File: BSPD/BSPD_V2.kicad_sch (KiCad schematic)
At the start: 36 parts, among them J1 Conn_01x02_Socket, J2 Conn_01x02_Socket, J3 Conn_01x02_Socket, J4 Conn_01x02_Socket, K1 Fujitsu_FTR-LYCA005x, Q2 NPN, Q3 IRF540N, Q4 NPN, U1 74LS02, U2 74LS08, U3 LM393, U5 LM393

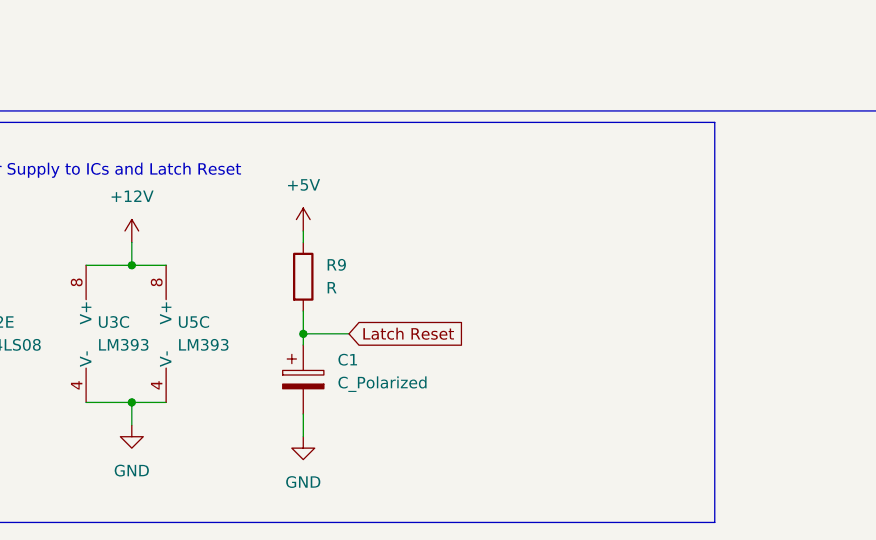
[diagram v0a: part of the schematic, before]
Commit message: Added a bypass capacitor to the supply of the comparators as stated by the Datasheet.
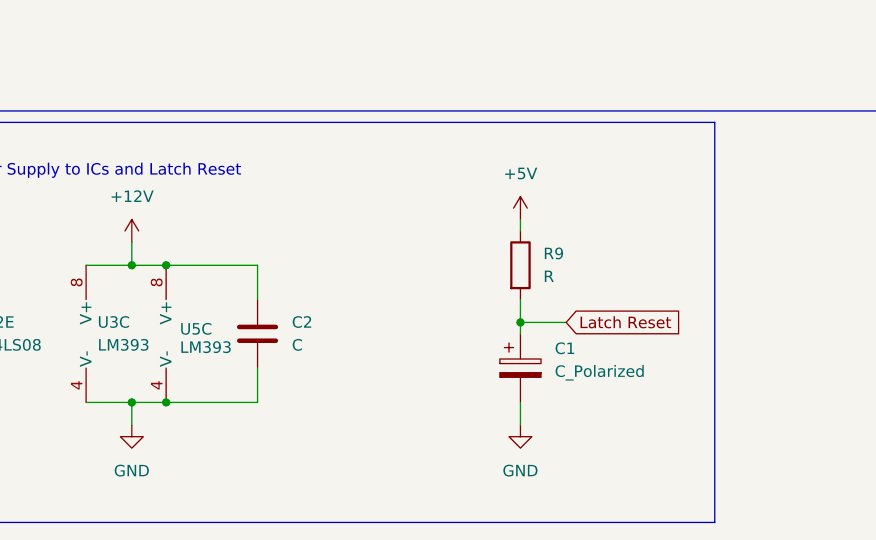
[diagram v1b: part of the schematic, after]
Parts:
- added C2: C, symbol Device:C
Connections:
- net +12V: now also C2.1
- net GND: now also C2.2
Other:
- moved on the sheet: C1, R9
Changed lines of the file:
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@@
 	)
 	(junction
+		(at 69.85 182.88)
+		(diameter 0)
+		(color 0 0 0 0)
+	)
+	(junction
 		(at 200.66 46.99)
 		(diameter 0)
@@
 	)
 	(junction
-		(at 85.09 175.26)
+		(at 69.85 167.64)
+		(diameter 0)
+		(color 0 0 0 0)
+	)
+	(junction
+		(at 109.22 173.99)
 		(diameter 0)
 		(color 0 0 0 0)
@@
 	(wire
 		(pts
-			(xy 85.09 175.26) (xy 85.09 176.53)
+			(xy 109.22 173.99) (xy 109.22 175.26)
 		)
 		(stroke
@@
 	(wire
 		(pts
+			(xy 69.85 167.64) (xy 80.01 167.64)
+		)
+		(stroke
+			(width 0)
+			(type default)
+		)
+	)
+	(wire
+		(pts
 			(xy 34.29 187.96) (xy 43.18 187.96)
 		)
@@
 	(wire
 		(pts
-			(xy 85.09 184.15) (xy 85.09 186.69)
+			(xy 109.22 182.88) (xy 109.22 185.42)
 		)
 		(stroke
@@
 	(wire
 		(pts
-			(xy 85.09 175.26) (xy 90.17 175.26)
+			(xy 109.22 173.99) (xy 114.3 173.99)
 		)
 		(stroke
@@
 	(wire
 		(pts
-			(xy 85.09 163.83) (xy 85.09 165.1)
+			(xy 109.22 162.56) (xy 109.22 163.83)
 		)
 		(stroke
@@
 	(wire
 		(pts
-			(xy 85.09 172.72) (xy 85.09 175.26)
+			(xy 109.22 171.45) (xy 109.22 173.99)
 		)
 		(stroke
@@
 	(wire
 		(pts
+			(xy 69.85 182.88) (xy 80.01 182.88)
+		)
+		(stroke
+			(width 0)
+			(type default)
+		)
+	)
+	(wire
+		(pts
 			(xy 191.77 154.94) (xy 194.31 154.94)
 		)
@@
 	(wire
 		(pts
+			(xy 80.01 167.64) (xy 80.01 171.45)
+		)
+		(stroke
+			(width 0)
+			(type default)
+		)
+	)
+	(wire
+		(pts
 			(xy 30.48 107.95) (xy 40.64 107.95)
 		)
@@
 	(wire
 		(pts
+			(xy 80.01 179.07) (xy 80.01 182.88)
+		)
+		(stroke
+			(width 0)
+			(type default)
+		)
+	)
+	(wire
+		(pts
 			(xy 116.84 104.14) (xy 116.84 106.68)
 		)
@@
 	(global_label "Latch Reset"
 		(shape input)
-		(at 90.17 175.26 0)
+		(at 114.3 173.99 0)
 		(fields_autoplaced yes)
 		(effects
@@
 		)
 		(property "Intersheetrefs" "${INTERSHEET_REFS}"
-			(at 104.4642 175.26 0)
+			(at 128.5942 173.99 0)
 			(effects
 				(font
@@
 	)
 	(symbol
+		(lib_id "Device:C")
+		(at 80.01 175.26 0)
+		(unit 1)
+		(exclude_from_sim no)
+		(in_bom yes)
+		(on_board yes)
+		(dnp no)
+		(fields_autoplaced yes)
+		(property "Reference" "C2"
+			(at 83.82 173.9899 0)
+			(effects
+				(font
+					(size 1.27 1.27)
+				)
+				(justify left)
+			)
+		)
+		(property "Value" "C"
+			(at 83.82 176.5299 0)
+			(effects
+				(font
+					(size 1.27 1.27)
+				)
+				(justify left)
+			)
+		)
+		(property "Footprint" ""
+			(at 80.9752 179.07 0)
+			(effects
+				(font
+					(size 1.27 1.27)
+				)
+				(hide yes)
+			)
+		)
+		(property "Datasheet" "~"
+			(at 80.01 175.26 0)
+			(effects
+				(font
+					(size 1.27 1.27)
+				)
+				(hide yes)
+			)
+		)
+		(property "Description" "Unpolarized capacitor"
+			(at 80.01 175.26 0)
+			(effects
+				(font
+					(size 1.27 1.27)
+				)
+				(hide yes)
+			)
+		)
+		(pin "1"
+		)
+		(pin "2"
+		)
+		(instances
+			(project ""
+				(path "/d92b65b7-5ac6-4942-9c7f-8311f0326af7"
+					(reference "C2")
+					(unit 1)
+				)
+			)
+		)
+	)
+	(symbol
 		(lib_id "power:+12V")
 		(at 232.41 22.86 0)
@@
 	(symbol
 		(lib_id "power:GND")
-		(at 85.09 186.69 0)
+		(at 109.22 185.42 0)
 		(unit 1)
 		(exclude_from_sim no)
@@
 		(fields_autoplaced yes)
 		(property "Reference" "#PWR010"
-			(at 85.09 193.04 0)
+			(at 109.22 191.77 0)
 			(effects
 				(font
@@
 		)
 		(property "Value" "GND"
-			(at 85.09 191.77 0)
+			(at 109.22 190.5 0)
 			(effects
 				(font
@@
 		)
 		(property "Footprint" ""
-			(at 85.09 186.69 0)
+			(at 109.22 185.42 0)
 			(effects
 				(font
@@
 		)
 		(property "Datasheet" ""
-			(at 85.09 186.69 0)
+			(at 109.22 185.42 0)
 			(effects
 				(font
@@
 		)
 		(property "Description" "Power symbol creates a global label with name \"GND\" , ground"
-			(at 85.09 186.69 0)
+			(at 109.22 185.42 0)
 			(effects
 				(font
@@
 	(symbol
 		(lib_id "power:+5V")
-		(at 85.09 163.83 0)
+		(at 109.22 162.56 0)
 		(unit 1)
 		(exclude_from_sim no)
@@
 		(fields_autoplaced yes)
 		(property "Reference" "#PWR09"
-			(at 85.09 167.64 0)
+			(at 109.22 166.37 0)
 			(effects
 				(font
@@
 		)
 		(property "Value" "+5V"
-			(at 85.09 158.75 0)
+			(at 109.22 157.48 0)
 			(effects
 				(font
@@
 		)
 		(property "Footprint" ""
-			(at 85.09 163.83 0)
+			(at 109.22 162.56 0)
 			(effects
 				(font
@@
 		)
 		(property "Datasheet" ""
-			(at 85.09 163.83 0)
+			(at 109.22 162.56 0)
 			(effects
 				(font
@@
 		)
 		(property "Description" "Power symbol creates a global label with name \"+5V\""
-			(at 85.09 163.83 0)
+			(at 109.22 162.56 0)
 			(effects
 				(font
@@
 	(symbol
 		(lib_id "Device:R")
-		(at 85.09 168.91 0)
+		(at 109.22 167.64 0)
 		(unit 1)
 		(exclude_from_sim no)
@@
 		(fields_autoplaced yes)
 		(property "Reference" "R9"
-			(at 87.63 167.6399 0)
+			(at 111.76 166.3699 0)
 			(effects
 				(font
@@
 		)
 		(property "Value" "R"
-			(at 87.63 170.1799 0)
+			(at 111.76 168.9099 0)
 			(effects
 				(font
@@
 		)
 		(property "Footprint" ""
-			(at 83.312 168.91 90)
+			(at 107.442 167.64 90)
 			(effects
 				(font
@@
 		)
 		(property "Datasheet" "~"
-			(at 85.09 168.91 0)
+			(at 109.22 167.64 0)
 			(effects
 				(font
@@
 		)
 		(property "Description" "Resistor"
-			(at 85.09 168.91 0)
+			(at 109.22 167.64 0)
 			(effects
 				(font
@@
 	(symbol
 		(lib_id "Device:C_Polarized")
-		(at 85.09 180.34 0)
+		(at 109.22 179.07 0)
 		(unit 1)
 		(exclude_from_sim no)
@@
 		(fields_autoplaced yes)
 		(property "Reference" "C1"
-			(at 88.9 178.1809 0)
+			(at 113.03 176.9109 0)
 			(effects
 				(font
@@
 		)
 		(property "Value" "C_Polarized"
-			(at 88.9 180.7209 0)
+			(at 113.03 179.4509 0)
 			(effects
 				(font
@@
 		)
 		(property "Footprint" ""
-			(at 86.0552 184.15 0)
+			(at 110.1852 182.88 0)
 			(effects
 				(font
@@
 		)
 		(property "Datasheet" "~"
-			(at 85.09 180.34 0)
+			(at 109.22 179.07 0)
 			(effects
 				(font
@@
 		)
 		(property "Description" "Polarized capacitor"
-			(at 85.09 180.34 0)
+			(at 109.22 179.07 0)
 			(effects
 				(font
@@
 		(on_board yes)
 		(dnp no)
-		(fields_autoplaced yes)
 		(property "Reference" "U5"
-			(at 71.12 173.9899 0)
+			(at 71.374 174.752 0)
 			(effects
 				(font
@@
 		)
 		(property "Value" "LM393"
-			(at 71.12 176.5299 0)
+			(at 71.374 176.784 0)
 			(effects
 				(font

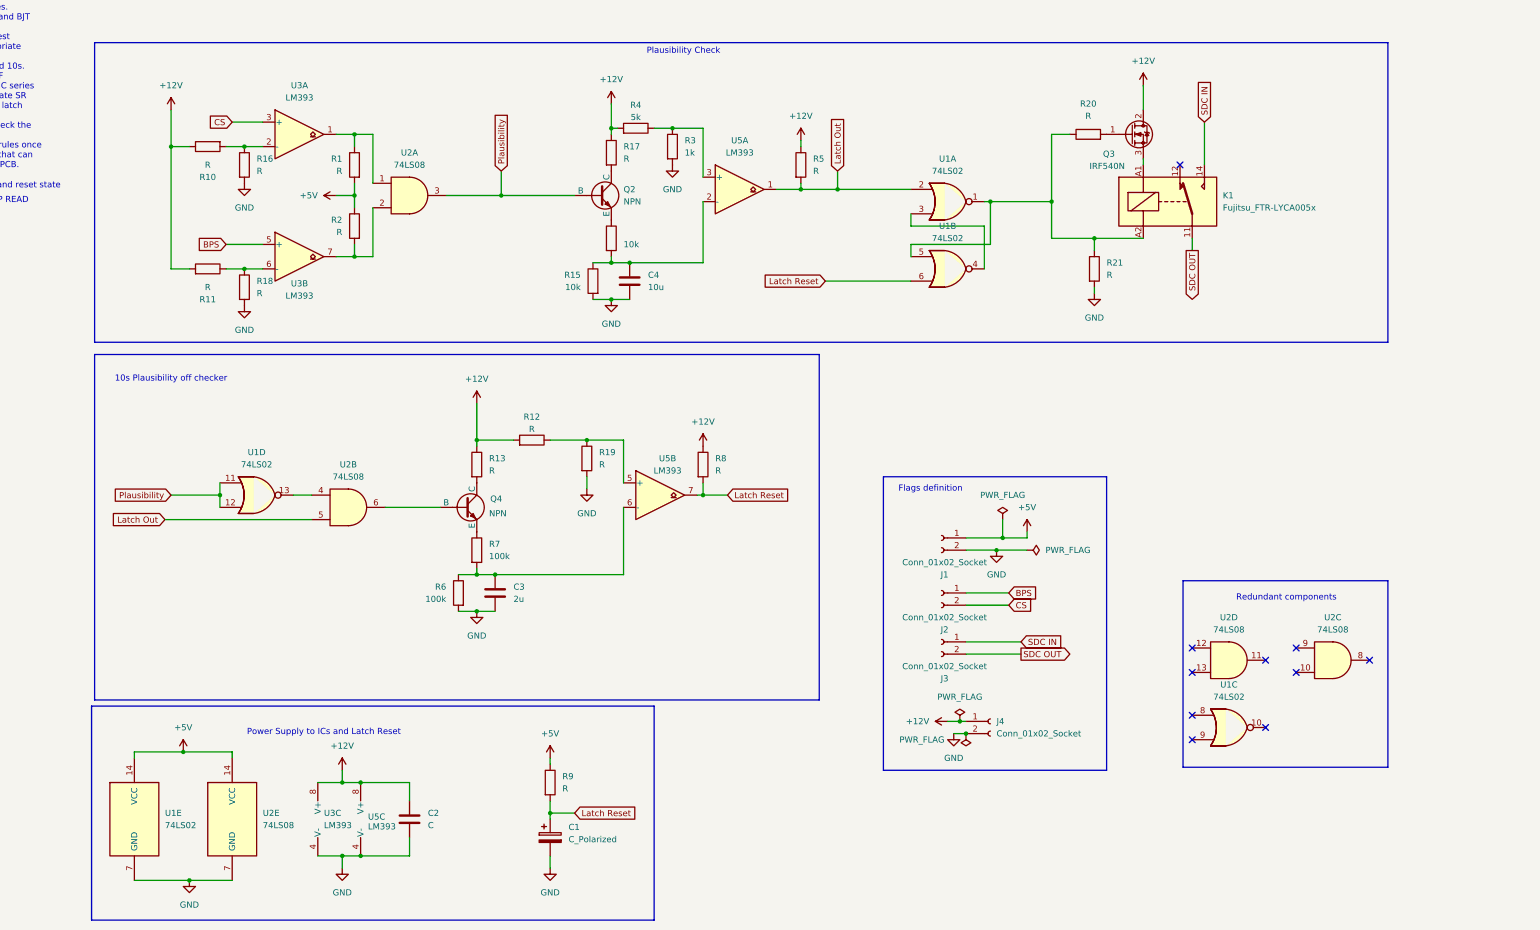
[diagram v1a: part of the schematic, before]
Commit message: Added a CD4081BM in place of regular LS AND gates, reason being better Voltage Supply range(3V-18V) which allows it to use the GLV power supply directly. Also, lower Tp. Had to add some flags as the symbol didn't break up into individual gates.
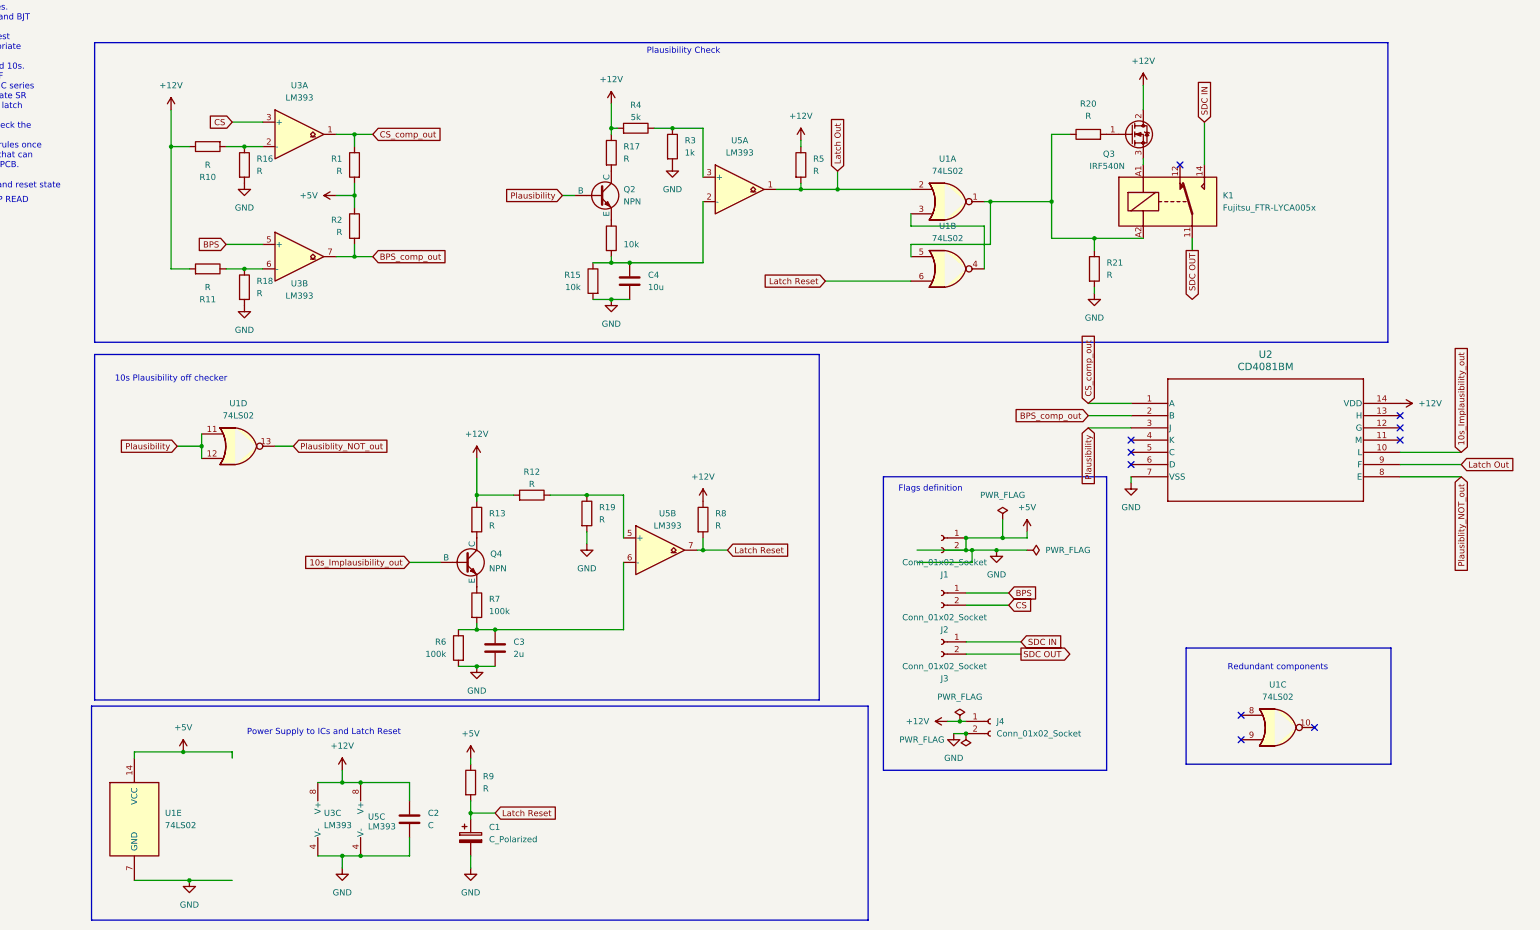
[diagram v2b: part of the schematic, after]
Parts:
- removed U2: 74LS08, symbol 74xx:74LS08
- added U2: CD4081BM, D14, symbol CD4081B:CD4081BM
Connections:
- net GND is gone; now on net +5V: C1.2, C2.2, C3.2, C4.2, J1.2 (Pin_2), J4.2 (Pin_2), R15.2, R16.2, R18.2, R19.2, R21.2, R3.2, R6.2, U1.7 (GND), U3.4 (V-), U5.4 (V-)
- net +12V: now also U2.14 (VDD)
- net +5V: now also U2.7 (VSS)
- net Latch Out: now also U2.9 (F)
- net Plausibility: now also U2.3 (J)
- net CS_comp_out: now reaches R1.1, U3.1
- net CS_comp_out: now also U2.1 (A)
- net 10s_Implausibility_out: now reaches Q4.2 (B)
- net 10s_Implausibility_out: now also U2.10 (L)
- net Plausiblity_NOT_out: now reaches U1.13
- net Plausiblity_NOT_out: now also U2.8 (E)
- net BPS_comp_out: now reaches R2.2, U3.7
- net BPS_comp_out: now also U2.2 (B)
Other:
- moved on the sheet: C1, C3, Q4, R12, R13, R19, R6, R7, R8, R9, U1C, U1D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

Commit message: Added the higher voltage NOR gate CD4001B IC, cleaned the schematic, and also added the inputs/ouputs to the symbols of the imported ics (CD4001B and CD40081B). Removed all +5V pins from the schematic.
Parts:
- removed J1: Conn_01x02_Socket, symbol Connector:Conn_01x02_Socket
- removed U1: 74LS02, symbol 74xx:74LS02
- removed U2: CD4081BM, D14, symbol CD4081B:CD4081BM
- added U1, U2: CD4001BM, D14, symbol CD4001B:CD4001BM
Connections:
- net +12V: now also R1.2, R2.1, R9.1, U1.14 (VDD), U2.14 (VDD)
- net 10s_Implausibility_out: now also U2.10 (L)
- net BPS_comp_out: now also U2.2 (B)
- net CS_comp_out: now also U2.1 (A)
- net Latch Out: now also U1.1 (A), U2.9 (F)
- net Latch Reset: now also U1.6 (D)
- net Plausibility: now also U1.8 (E), U1.9 (F), U2.3 (J)
- net Plausiblity_NOT_out: now also U1.10 (L), U2.8 (E)
- net Q_ouput: now reaches K1.A2, R20.1, R21.1
- net Q_ouput: now also U1.3 (J), U1.5 (C)
- net +5V renamed GND
- net GND: now also U1.7 (VSS), U2.7 (VSS); no longer R1.2, R2.1, R9.1
- new net: U1.2 (B), U1.4 (K)
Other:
- note added: "1)Check the voltage divider values for 2.2V to 10.5V from CS. 2)Get the pullup resistor values. 3)Compare between MOSFET and BJT as switch. 4)Check for whatever is the best and for that place the appropriate resistors to bias them. 5)Verify the time of 500ms and 10s. Keep capacitor value of 0.1uF 7)Look into reset for the nor gate SR Latch. 8)After finishing the above, check the logic once again.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"
- note added: "AND GATE"
- note added: "NOR GATE"
- note removed: "1)Check the voltage divider values for 2.2V to 10.5V from CS. 2)Get the pullup resistor values. 3)Compare between MOSFET and BJT as switch. 4)Check for whatever is the best and for that place the appropriate resistors to bias them. 5)Verify the time of 500ms and 10s. Keep capacitor value of 0.1uF 6)Replace the LS series with HC series 7)Look into reset for the nor gate SR Latch. If possible, repl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"
- note removed: "Redundant components"
- note removed: "Relay and reset state"
- note removed: "SCS IMP READ"
- moved on the sheet: C1, C2, C3, C4, J2, J3, J4, K1, Q2, Q3, Q4, R1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

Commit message: Changed the PS capcitor value to 1uF, it should be enough for removing inconsistencies in the GLV supply. Also set the pulldown resistor value to 1 ohm, it needs to be as small as possible to keep the SR state zero as fast as possible, this may need to be revised depending on the review
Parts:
- removed Q2: NPN, symbol Simulation_SPICE:NPN
- added Q1: NPN, symbol Simulation_SPICE:NPN
- C2: value C -> 1uF
- R21: value R -> 1
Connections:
- net Plausibility: now also Q1.2 (B)
- net at R17.2: now also Q1.1 (C)
- net at R14.1: now also Q1.3 (E)
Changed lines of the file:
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@@
 	(wire
 		(pts
-			(xy 137.16 69.85) (xy 139.7 69.85)
+			(xy 127 69.85) (xy 139.7 69.85)
 		)
 		(stroke
@@
 	(global_label "Plausibility"
 		(shape input)
-		(at 137.16 69.85 180)
+		(at 127 69.85 180)
 		(fields_autoplaced yes)
 		(effects
@@
 		)
 		(property "Intersheetrefs" "${INTERSHEET_REFS}"
-			(at 123.5916 69.85 0)
+			(at 113.4316 69.85 0)
 			(effects
 				(font
@@
 			)
 		)
-		(property "Value" "C"
+		(property "Value" "1uF"
 			(at 64.77 207.0099 0)
 			(effects
@@
 	(symbol
 		(lib_id "Simulation_SPICE:NPN")
-		(at 144.78 69.85 0)
-		(unit 1)
-		(exclude_from_sim no)
-		(in_bom yes)
-		(on_board yes)
-		(dnp no)
-		(fields_autoplaced yes)
-		(property "Reference" "Q2"
-			(at 149.86 68.5799 0)
-			(effects
-				(font
-					(size 1.27 1.27)
-				)
-				(justify left)
-			)
-		)
-		(property "Value" "NPN"
-			(at 149.86 71.1199 0)
-			(effects
-				(font
-					(size 1.27 1.27)
-				)
-				(justify left)
-			)
-		)
-		(property "Footprint" ""
-			(at 208.28 69.85 0)
-			(effects
-				(font
-					(size 1.27 1.27)
-				)
-				(hide yes)
-			)
-		)
-		(property "Datasheet" "https://ngspice.sourceforge.io/docs/ngspice-html-manual/manual.xhtml#cha_BJTs"
-			(at 208.28 69.85 0)
-			(effects
-				(font
-					(size 1.27 1.27)
-				)
-				(hide yes)
-			)
-		)
-		(property "Description" "Bipolar transistor symbol for simulation only, substrate tied to the emitter"
-			(at 144.78 69.85 0)
-			(effects
-				(font
-					(size 1.27 1.27)
-				)
-				(hide yes)
-			)
-		)
-		(property "Sim.Device" "NPN"
-			(at 144.78 69.85 0)
-			(effects
-				(font
-					(size 1.27 1.27)
-				)
-				(hide yes)
-			)
-		)
-		(property "Sim.Type" "GUMMELPOON"
-			(at 144.78 69.85 0)
-			(effects
-				(font
-					(size 1.27 1.27)
-				)
-				(hide yes)
-			)
-		)
-		(property "Sim.Pins" "1=C 2=B 3=E"
-			(at 144.78 69.85 0)
-			(effects
-				(font
-					(size 1.27 1.27)
-				)
-				(hide yes)
-			)
-		)
-		(pin "3"
-		)
-		(pin "2"
-		)
-		(pin "1"
-		)
-		(instances
-			(project ""
-				(path "/d92b65b7-5ac6-4942-9c7f-8311f0326af7"
-					(reference "Q2")
-					(unit 1)
-				)
-			)
-		)
-	)
-	(symbol
-		(lib_id "Simulation_SPICE:NPN")
 		(at 69.85 146.05 0)
 		(unit 1)
@@
 	)
 	(symbol
+		(lib_id "Simulation_SPICE:NPN")
+		(at 144.78 69.85 0)
+		(unit 1)
+		(exclude_from_sim no)
+		(in_bom yes)
+		(on_board yes)
+		(dnp no)
+		(fields_autoplaced yes)
+		(property "Reference" "Q1"
+			(at 149.86 68.5799 0)
+			(effects
+				(font
+					(size 1.27 1.27)
+				)
+				(justify left)
+			)
+		)
+		(property "Value" "NPN"
+			(at 149.86 71.1199 0)
+			(effects
+				(font
+					(size 1.27 1.27)
+				)
+				(justify left)
+			)
+		)
+		(property "Footprint" ""
+			(at 208.28 69.85 0)
+			(effects
+				(font
+					(size 1.27 1.27)
+				)
+				(hide yes)
+			)
+		)
+		(property "Datasheet" "https://ngspice.sourceforge.io/docs/ngspice-html-manual/manual.xhtml#cha_BJTs"
+			(at 208.28 69.85 0)
+			(effects
+				(font
+					(size 1.27 1.27)
+				)
+				(hide yes)
+			)
+		)
+		(property "Description" "Bipolar transistor symbol for simulation only, substrate tied to the emitter"
+			(at 144.78 69.85 0)
+			(effects
+				(font
+					(size 1.27 1.27)
+				)
+				(hide yes)
+			)
+		)
+		(property "Sim.Device" "NPN"
+			(at 144.78 69.85 0)
+			(effects
+				(font
+					(size 1.27 1.27)
+				)
+				(hide yes)
+			)
+		)
+		(property "Sim.Type" "GUMMELPOON"
+			(at 144.78 69.85 0)
+			(effects
+				(font
+					(size 1.27 1.27)
+				)
+				(hide yes)
+			)
+		)
+		(property "Sim.Pins" "1=C 2=B 3=E"
+			(at 144.78 69.85 0)
+			(effects
+				(font
+					(size 1.27 1.27)
+				)
+				(hide yes)
+			)
+		)
+		(pin "3"
+		)
+		(pin "1"
+		)
+		(pin "2"
+		)
+		(instances
+			(project ""
+				(path "/d92b65b7-5ac6-4942-9c7f-8311f0326af7"
+					(reference "Q1")
+					(unit 1)
+				)
+			)
+		)
+	)
+	(symbol
 		(lib_id "Device:R")
 		(at 147.32 78.74 0)
@@
 			)
 		)
-		(property "Value" "R"
+		(property "Value" "1"
 			(at 242.57 86.3599 0)
 			(effects

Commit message: Added 10k pullup resistors, these are more than enough with a minimal current of +- 1.2 mA, flowing through them. This current won't also damage the components. Verification is still recommended
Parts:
- removed Q1, Q4: NPN, symbol Simulation_SPICE:NPN
- removed Q3: IRF540N, Package_TO_SOT_THT:TO-220-3_Vertical, symbol Transistor_FET:IRF540N
- removed R13, R17, R20: R, symbol Device:R
- added Q1, Q2, Q3: NMOS, symbol Simulation_SPICE:NMOS
- R1, R2, R5, R8: value R -> 10k
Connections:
- net +12V: now also Q1.1 (D), Q2.1 (D), Q3.1 (D)
- net 10s_Implausibility_out: now also Q3.2 (G)
- net Plausibility: now also Q1.2 (G)
- net Q_ouput: now also Q2.2 (G)
- net at R7.1: now also Q3.3 (S)
- net at R14.1: now also Q1.3 (S)
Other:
- moved on the sheet: R19, R5
